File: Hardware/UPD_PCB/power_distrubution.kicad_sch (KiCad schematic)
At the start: 40 parts, among them Q1 LMR51635XDDCR, Q2 LMR51635XDDCR, Q3 LMR51635XDDCR, Q4 LMR51635XDDCR, Q5 LMR51635XDDCR

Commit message: Updated design
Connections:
- net +12V_out renamed +12V
- net +16V_out renamed +16V
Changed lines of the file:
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@@
 		)
 	)
-	(label "+12V_out"
+	(label "+12V"
 		(at 190.5 62.23 180)
 		(fields_autoplaced yes)
@@
 		)
 	)
-	(label "+16V_out"
+	(label "+16V"
 		(at 271.78 62.23 180)
 		(fields_autoplaced yes)
@@
 		)
 	)
-	(label "+5V_out"
+	(label "+5V"
 		(at 189.23 107.95 180)
 		(fields_autoplaced yes)

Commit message: Finalized Schematic
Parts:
- removed C5: C, symbol Device:C
- removed L1, L2, L3, L4, L5: L, symbol Device:L
- removed R7: 10k2, symbol Device:R
- removed R9: 143k, symbol Device:R
- added C21, C22: DNP, Capacitor_SMD:C_0603_1608Metric_Pad1.08x0.95mm_HandSolder, symbol Device:C
- added C23, C24: 0.1µF, Capacitor_SMD:C_0603_1608Metric_Pad1.08x0.95mm_HandSolder, symbol Device:C
- added C25, C7: 22µF, Capacitor_SMD:CP_Elec_6.3x5.8, symbol Device:C
- added C26, C27: 33µF, Capacitor_SMD:CP_Elec_6.3x5.8, symbol Device:C
- added L1, L3, L5: 33µH, INDPM140128X650N, symbol PA4343_153NLT:PA4343.153NLT
- added L2, L4: 22µH, INDPM140128X650N, symbol PA4343_153NLT:PA4343.153NLT
- added L6: 15µH, INDPM140128X650N, symbol PA4343_153NLT:PA4343.153NLT
- added Q4: LMR51635XDDCR, SOT95P280X110-6N, symbol LMR51635XDDCR:LMR51635XDDCR
- added R4, R8: 143k, Resistor_SMD:R_0603_1608Metric_Pad0.98x0.95mm_HandSolder, symbol Device:R
- added R5, R6: 10k2, Resistor_SMD:R_0603_1608Metric_Pad0.98x0.95mm_HandSolder, symbol Device:R
- C1, C10, C11, C19, C2, C20: value C -> 2.2µF; footprint (none) -> Capacitor_SMD:C_0603_1608Metric_Pad1.08x0.95mm_HandSolder
- C12, C13, C3, C4: value C -> DNP; footprint (none) -> Capacitor_SMD:C_0603_1608Metric_Pad1.08x0.95mm_HandSolder
- C14, C15, C6: value C -> 0.1µF; footprint (none) -> Capacitor_SMD:C_0603_1608Metric_Pad1.08x0.95mm_HandSolder
- C16, C18, C9: value C -> 22µF; footprint (none) -> Capacitor_SMD:CP_Elec_6.3x5.8
- C17, C8: value C -> 10µF; footprint (none) -> Capacitor_SMD:CP_Elec_6.3x5.8
- C5: renamed from C7; value C -> 0.1µF; footprint (none) -> Capacitor_SMD:C_0603_1608Metric_Pad1.08x0.95mm_HandSolder
- renumbered Q4 to Q2, Q2 to Q3, Q3 to Q5, Q5 to Q6, R8 to R10, R6 to R11, R10 to R12, R4 to R3, R5 to R7, R3 to R9
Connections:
- net +12V is gone; now on net GND: C19.2
- net +16V: now also C21.2, C25.2, L5.2; no longer C12.2
- net +19V: now also C12.2, C16.2, L3.2; no longer C11.2
- net +24V: now also C3.2, C7.2, L1.2; no longer C10.2
- net +42V: now also C1.1, C10.1, C11.1, C19.1, C2.1, C20.1, Q4.2 (EN), Q4.3 (VIN); no longer C15.1, C16.1, C4.1, C6.1
- net GND: now also C1.2, C10.2, C11.2, C16.1, C17.1, C18.1, C2.2, C20.2, C8.1, C9.1, C25.1, C26.1, C27.1, C7.1, Q4.4 (GND), R5.2, R6.2; no longer C1.1, C10.1, C11.1, C12.1, C13.1, C14.1, C15.2, C16.2, C19.1, C2.1, C20.1, C3.1, C4.2, C6.2
- net at Q5.1 (FB), R11.2, R9.1: now also C21.1; no longer C3.2
- net at Q1.1 (FB), R1.1, R3.2: now also C3.1; no longer C1.2
- net at Q3.1 (FB), R7.2: now also C12.1, R5.1; no longer C2.2, R2.1
- net at Q6.1 (FB), R10.1, R12.2: now also C22.1; no longer C14.2
- net at Q5.6 (CB): now also C23.1; no longer C9.1
- net at Q5.5 (SW): now also C23.2, L5.1; no longer C9.2
- net at Q3.6 (CB): now also C14.1; no longer C8.1
- net at Q3.5 (SW): now also C14.2, L3.1; no longer C8.2
- net at Q2.1 (FB): now also C4.1, R2.1, R4.2; no longer C13.2
- net at Q6.5 (SW): now also C24.2, L6.1; no longer C18.2
- net at C5.2, Q1.5 (SW): now also L1.1
- net at Q2.5 (SW): now also C6.2, L2.1; no longer C17.2
- net at Q2.6 (CB): now also C6.1; no longer C17.1
- net at Q6.6 (CB): now also C24.1; no longer C18.1
- net +5V renamed +5V_NS
- net +5V_NS: now also C22.2, C26.2, C27.2, L6.2; no longer C20.2
- new net: C13.1, Q4.1 (FB), R6.1, R8.2
- new net: C15.2, L4.1, Q4.5 (SW)
- new net: C15.1, Q4.6 (CB)
- new net +12V_1: C4.2, C8.2, C9.2, L2.2, R4.1
- new net +12V_2: C13.2, C17.2, C18.2, L4.2, R8.1
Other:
- moved on the sheet: Q2, Q3, Q6, R10, R12, R7

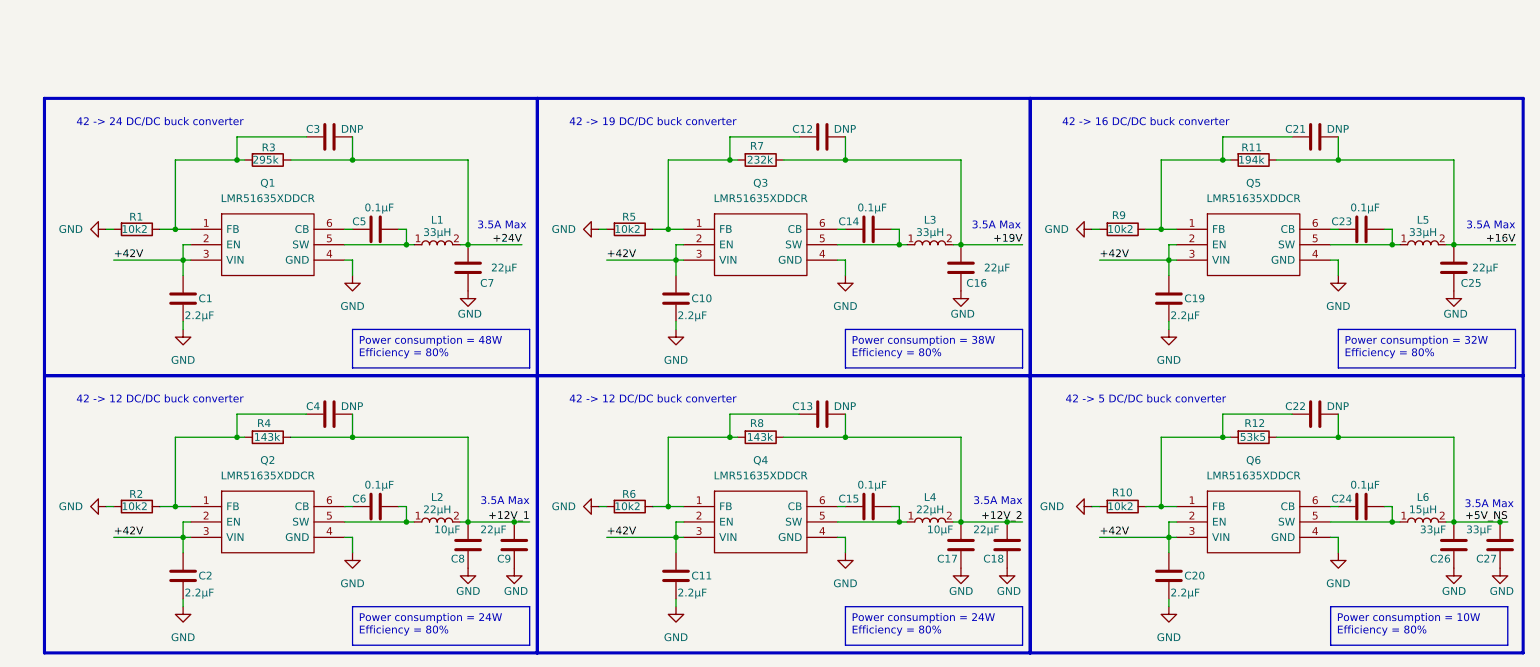
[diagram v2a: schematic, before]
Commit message: Pcb layout before changing inductor
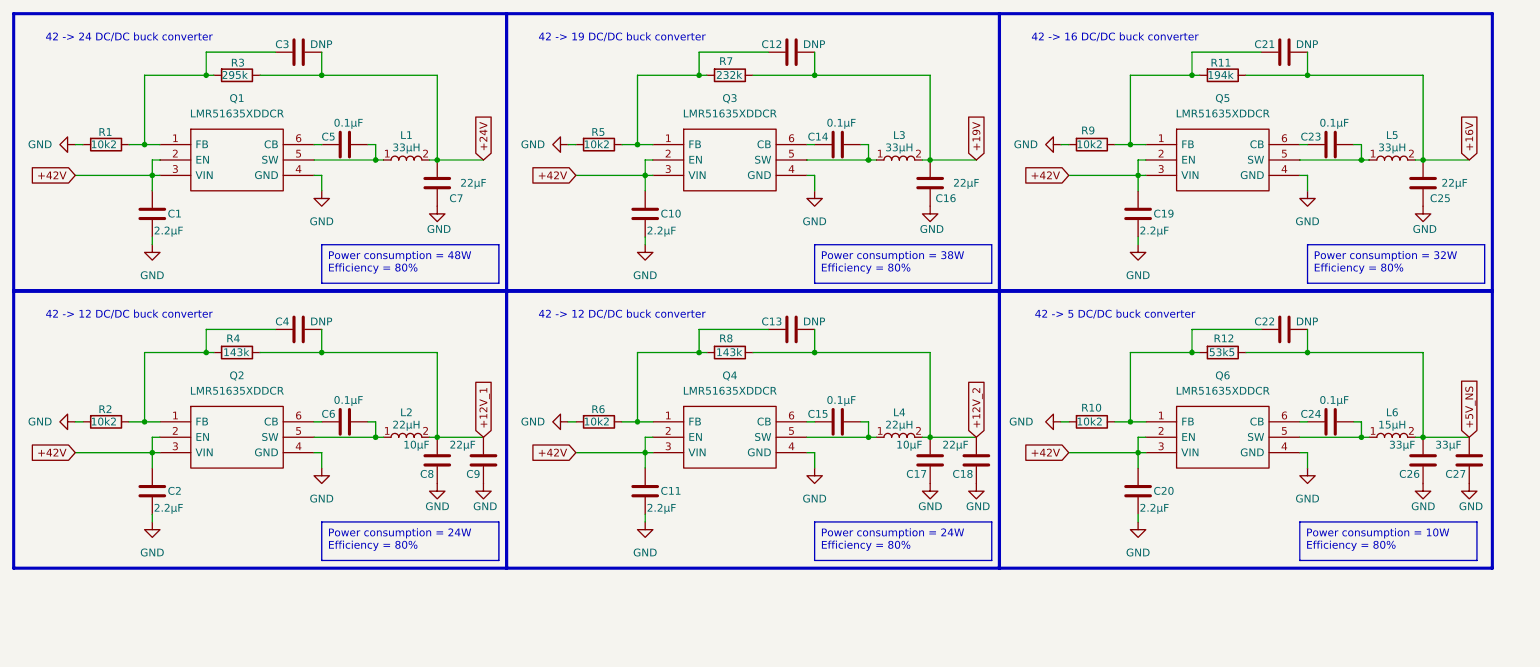
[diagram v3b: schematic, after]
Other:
- note removed: "3.5A Max"
- moved on the sheet: C1, C10, C11, C12, C13, C14, C15, C16, C17, C18, C19, C2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

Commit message: Finalized PCB
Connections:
- net +12V_1: now also C8.1, C9.1; no longer C8.2, C9.2
- net +12V_2: now also C17.1, C18.1; no longer C17.2, C18.2
- net +16V: now also C25.1; no longer C25.2
- net +19V: now also C16.1; no longer C16.2
- net +24V: now also C7.1; no longer C7.2
- net +5V_NS: now also C26.1, C27.1; no longer C26.2, C27.2
- net GND: now also C16.2, C17.2, C18.2, C25.2, C26.2, C27.2, C7.2, C8.2, C9.2; no longer C16.1, C17.1, C18.1, C25.1, C26.1, C27.1, C7.1, C8.1, C9.1
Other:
- moved on the sheet: C16, C17, C18, C25, C26, C27, C7, C8, C9
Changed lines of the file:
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@@
 	)
 	(rectangle
-		(start 186.69 24.13)
-		(end 267.97 69.85)
+		(start 267.97 69.85)
+		(end 186.69 24.13)
 		(stroke
 			(width 0.508)
@@
 	(symbol
 		(lib_id "Device:C")
-		(at 93.98 52.07 180)
+		(at 93.98 52.07 0)
 		(unit 1)
 		(exclude_from_sim no)
@@
 		(dnp no)
 		(property "Reference" "C7"
-			(at 98.298 54.61 0)
+			(at 89.662 49.53 0)
 			(effects
 				(font
@@
 		)
 		(property "Value" "22µF"
-			(at 102.108 52.07 0)
+			(at 85.852 52.07 0)
 			(effects
 				(font
@@
 		)
 		(property "Footprint" "Capacitor_SMD:CP_Elec_6.3x5.8"
-			(at 93.0148 48.26 0)
+			(at 94.9452 55.88 0)
 			(effects
 				(font
@@
 	(symbol
 		(lib_id "Device:C")
-		(at 175.26 97.79 180)
+		(at 175.26 97.79 0)
 		(unit 1)
 		(exclude_from_sim no)
@@
 		(dnp no)
 		(property "Reference" "C17"
-			(at 174.752 100.076 0)
+			(at 175.768 95.504 0)
 			(effects
 				(font
@@
 		)
 		(property "Value" "10µF"
-			(at 173.99 95.25 0)
+			(at 176.53 100.33 0)
 			(effects
 				(font
@@
 		)
 		(property "Footprint" "Capacitor_SMD:CP_Elec_6.3x5.8"
-			(at 174.2948 93.98 0)
+			(at 176.2252 101.6 0)
 			(effects
 				(font
@@
 	(symbol
 		(lib_id "Device:C")
-		(at 264.16 97.79 180)
+		(at 264.16 97.79 0)
 		(unit 1)
 		(exclude_from_sim no)
@@
 		(dnp no)
 		(property "Reference" "C27"
-			(at 263.652 100.076 0)
+			(at 264.668 95.504 0)
 			(effects
 				(font
@@
 		)
 		(property "Value" "33µF"
-			(at 262.89 95.25 0)
+			(at 265.43 100.33 0)
 			(effects
 				(font
@@
 		)
 		(property "Footprint" "Capacitor_SMD:CP_Elec_6.3x5.8"
-			(at 263.1948 93.98 0)
+			(at 265.1252 101.6 0)
 			(effects
 				(font
@@
 	(symbol
 		(lib_id "Device:C")
-		(at 93.98 97.79 180)
+		(at 93.98 97.79 0)
 		(unit 1)
 		(exclude_from_sim no)
@@
 		(dnp no)
 		(property "Reference" "C8"
-			(at 93.472 100.076 0)
+			(at 94.488 95.504 0)
 			(effects
 				(font
@@
 		)
 		(property "Value" "10µF"
-			(at 92.71 95.25 0)
+			(at 95.25 100.33 0)
 			(effects
 				(font
@@
 		)
 		(property "Footprint" "Capacitor_SMD:CP_Elec_6.3x5.8"
-			(at 93.0148 93.98 0)
+			(at 94.9452 101.6 0)
 			(effects
 				(font
@@
 	(symbol
 		(lib_id "Device:C")
-		(at 101.6 97.79 180)
+		(at 101.6 97.79 0)
 		(unit 1)
 		(exclude_from_sim no)
@@
 		(dnp no)
 		(property "Reference" "C9"
-			(at 101.092 100.076 0)
+			(at 102.108 95.504 0)
 			(effects
 				(font
@@
 		)
 		(property "Value" "22µF"
-			(at 100.33 95.25 0)
+			(at 102.87 100.33 0)
 			(effects
 				(font
@@
 		)
 		(property "Footprint" "Capacitor_SMD:CP_Elec_6.3x5.8"
-			(at 100.6348 93.98 0)
+			(at 102.5652 101.6 0)
 			(effects
 				(font
@@
 	(symbol
 		(lib_id "Device:C")
-		(at 175.26 52.07 180)
+		(at 175.26 52.07 0)
 		(unit 1)
 		(exclude_from_sim no)
@@
 		(dnp no)
 		(property "Reference" "C16"
-			(at 179.578 54.61 0)
+			(at 170.942 49.53 0)
 			(effects
 				(font
@@
 		)
 		(property "Value" "22µF"
-			(at 183.388 52.07 0)
+			(at 167.132 52.07 0)
 			(effects
 				(font
@@
 		)
 		(property "Footprint" "Capacitor_SMD:CP_Elec_6.3x5.8"
-			(at 174.2948 48.26 0)
+			(at 176.2252 55.88 0)
 			(effects
 				(font
@@
 	(symbol
 		(lib_id "Device:C")
-		(at 256.54 52.07 180)
+		(at 256.54 52.07 0)
 		(unit 1)
 		(exclude_from_sim no)
@@
 		(dnp no)
 		(property "Reference" "C25"
-			(at 261.112 54.61 0)
+			(at 251.968 49.53 0)
 			(effects
 				(font
@@
 		)
 		(property "Value" "22µF"
-			(at 263.906 52.07 0)
+			(at 249.174 52.07 0)
 			(effects
 				(font
@@
 		)
 		(property "Footprint" "Capacitor_SMD:CP_Elec_6.3x5.8"
-			(at 255.5748 48.26 0)
+			(at 257.5052 55.88 0)
 			(effects
 				(font
@@
 	(symbol
 		(lib_id "Device:C")
-		(at 256.54 97.79 180)
+		(at 256.54 97.79 0)
 		(unit 1)
 		(exclude_from_sim no)
@@
 		(dnp no)
 		(property "Reference" "C26"
-			(at 256.032 100.076 0)
+			(at 257.048 95.504 0)
 			(effects
 				(font
@@
 		)
 		(property "Value" "33µF"
-			(at 255.27 95.25 0)
+			(at 257.81 100.33 0)
 			(effects
 				(font
@@
 		)
 		(property "Footprint" "Capacitor_SMD:CP_Elec_6.3x5.8"
-			(at 255.5748 93.98 0)
+			(at 257.5052 101.6 0)
 			(effects
 				(font
@@
 	(symbol
 		(lib_id "Device:C")
-		(at 182.88 97.79 180)
+		(at 182.88 97.79 0)
 		(unit 1)
 		(exclude_from_sim no)
@@
 		(dnp no)
 		(property "Reference" "C18"
-			(at 182.372 100.076 0)
+			(at 183.388 95.504 0)
 			(effects
 				(font
@@
 		)
 		(property "Value" "22µF"
-			(at 181.61 95.25 0)
+			(at 184.15 100.33 0)
 			(effects
 				(font
@@
 		)
 		(property "Footprint" "Capacitor_SMD:CP_Elec_6.3x5.8"
-			(at 181.9148 93.98 0)
+			(at 183.8452 101.6 0)
 			(effects
 				(font
